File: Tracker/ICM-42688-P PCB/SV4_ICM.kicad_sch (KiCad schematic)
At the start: 18 parts, among them U1 SuperMini nRF52840, U2 ICM-42688-P, U3 MMC5983MA, U4 K3-1295S-E1

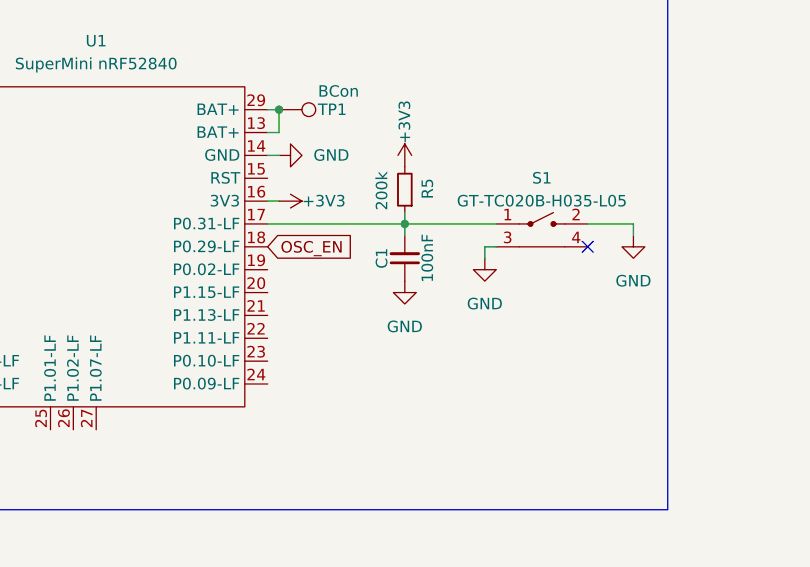
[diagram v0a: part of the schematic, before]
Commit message: - Added testing jig 3d model - Added folder for jigs - Removed debouncing capacitor from PCB, not needed.
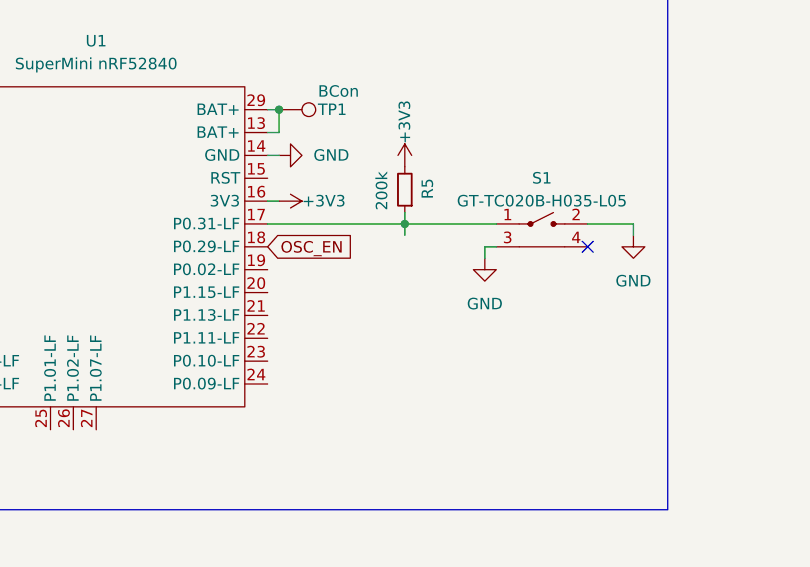
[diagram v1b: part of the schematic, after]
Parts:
- removed C1: 100nF, Capacitor_SMD:C_0402_1005Metric, symbol LSM6DSV Symbols:C_Small
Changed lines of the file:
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@@
-	(symbol
-		(lib_id "power:GND")
-		(at 107.95 68.58 0)
-		(unit 1)
-		(exclude_from_sim no)
-		(in_bom yes)
-		(on_board yes)
-		(dnp no)
-		(fields_autoplaced yes)
-		(property "Reference" "#PWR017"
-			(at 107.95 74.93 0)
-			(effects
-				(font
-					(size 1.27 1.27)
-				)
-				(hide yes)
-			)
-		)
-		(property "Value" "GND"
-			(at 107.95 73.66 0)
-			(effects
-				(font
-					(size 1.27 1.27)
-				)
-			)
-		)
-		(property "Footprint" ""
-			(at 107.95 68.58 0)
-			(effects
-				(font
-					(size 1.27 1.27)
-				)
-				(hide yes)
-			)
-		)
-		(property "Datasheet" ""
-			(at 107.95 68.58 0)
-			(effects
-				(font
-					(size 1.27 1.27)
-				)
-				(hide yes)
-			)
-		)
-		(property "Description" "Power symbol creates a global label with name \"GND\" , ground"
-			(at 107.95 68.58 0)
-			(effects
-				(font
-					(size 1.27 1.27)
-				)
-				(hide yes)
-			)
-		)
-		(pin "1"
-		)
-		(instances
-			(project "SV4"
-				(path "/a7c00f74-135d-49a9-8541-ca5663fb79a7"
-					(reference "#PWR017")
-					(unit 1)
-				)
-			)
-		)
-	)
 	(symbol
 		(lib_id "power:GND")
@@
 					(unit 1)
 				)
-			)
-		)
-	)
-	(symbol
-		(lib_id "LSM6DSV Symbols:C_Small")
-		(at 107.95 66.04 180)
-		(unit 1)
-		(exclude_from_sim no)
-		(in_bom yes)
-		(on_board yes)
-		(dnp no)
-		(property "Reference" "C1"
-			(at 105.41 66.04 90)
-			(effects
-				(font
-					(size 1.27 1.27)
-				)
-			)
-		)
-		(property "Value" "100nF"
-			(at 110.49 66.04 90)
-			(effects
-				(font
-					(size 1.27 1.27)
-				)
-			)
-		)
-		(property "Footprint" "Capacitor_SMD:C_0402_1005Metric"
-			(at 107.95 66.04 0)
-			(effects
-				(font
-					(size 1.27 1.27)
-				)
-				(hide yes)
-			)
-		)
-		(property "Datasheet" ""
-			(at 107.95 66.04 0)
-			(effects
-				(font
-					(size 1.27 1.27)
-				)
-				(hide yes)
-			)
-		)
-		(property "Description" ""
-			(at 107.95 66.04 0)
-			(effects
-				(font
-					(size 1.27 1.27)
-				)
-				(hide yes)
-			)
-		)
-		(property "MPN" "C14663"
-			(at 107.95 66.04 90)
-			(effects
-				(font
-					(size 1.27 1.27)
-				)
-				(hide yes)
-			)
-		)
-		(pin "2"
-		)
-		(pin "1"
-		)
-		(instances
-			(project "SV4"
-				(path "/a7c00f74-135d-49a9-8541-ca5663fb79a7"
-					(reference "C1")
-					(unit 1)
-				)

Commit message: - Started updating pcb for spi, didn't ifnish lol use the last commit - Added
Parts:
- removed C2: 1uF, Capacitor_SMD:C_0402_1005Metric, symbol LSM6DSV Symbols:C_Small
- removed C5: 10uF, Capacitor_SMD:C_0402_1005Metric, symbol LSM6DSV Symbols:C_Small
- removed C7: 2.2uF, Capacitor_SMD:C_0402_1005Metric, symbol LSM6DSV Symbols:C_Small
- removed R1, R2: 10k, Resistor_SMD:R_0402_1005Metric, symbol LSM6DSV Symbols:R_Small
- removed R5: 200k, Resistor_SMD:R_0402_1005Metric, symbol LSM6DSV Symbols:R_Small
- removed U3: MMC5983MA, mag_custom:MMC5983MA, symbol mag_custom:MMC5983MA
- C3: value 10nF -> 100nF
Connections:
- net +3V3: no longer U2.12 (AP_CS)
- net GND: no longer U2.1 (AP_SDO/AP_AD0)
- net OSC_EN: now also U1.22 (P1.11-LF); no longer U1.18 (P0.29-LF)
- net CLK: now reaches U2.9 (INT2/FSYNC/CLKIN), X1.3 (OUT)
- net CS: now reaches U1.6 (P0.20)
- net CS: now also U2.12 (AP_CS)
- new net SDO: U1.18 (P0.29-LF), U2.1 (AP_SDO/AP_AD0)
- no-connect marks 13 -> 5
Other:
- note added: "removed cause it used i2c! should switch to qmc."
- moved on the sheet: C8
